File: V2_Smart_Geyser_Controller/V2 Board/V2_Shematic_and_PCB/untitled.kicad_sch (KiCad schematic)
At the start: 5 parts, among them J2 1714984, K2 SLA-12VDC-SL-C, Q1 AO3400A

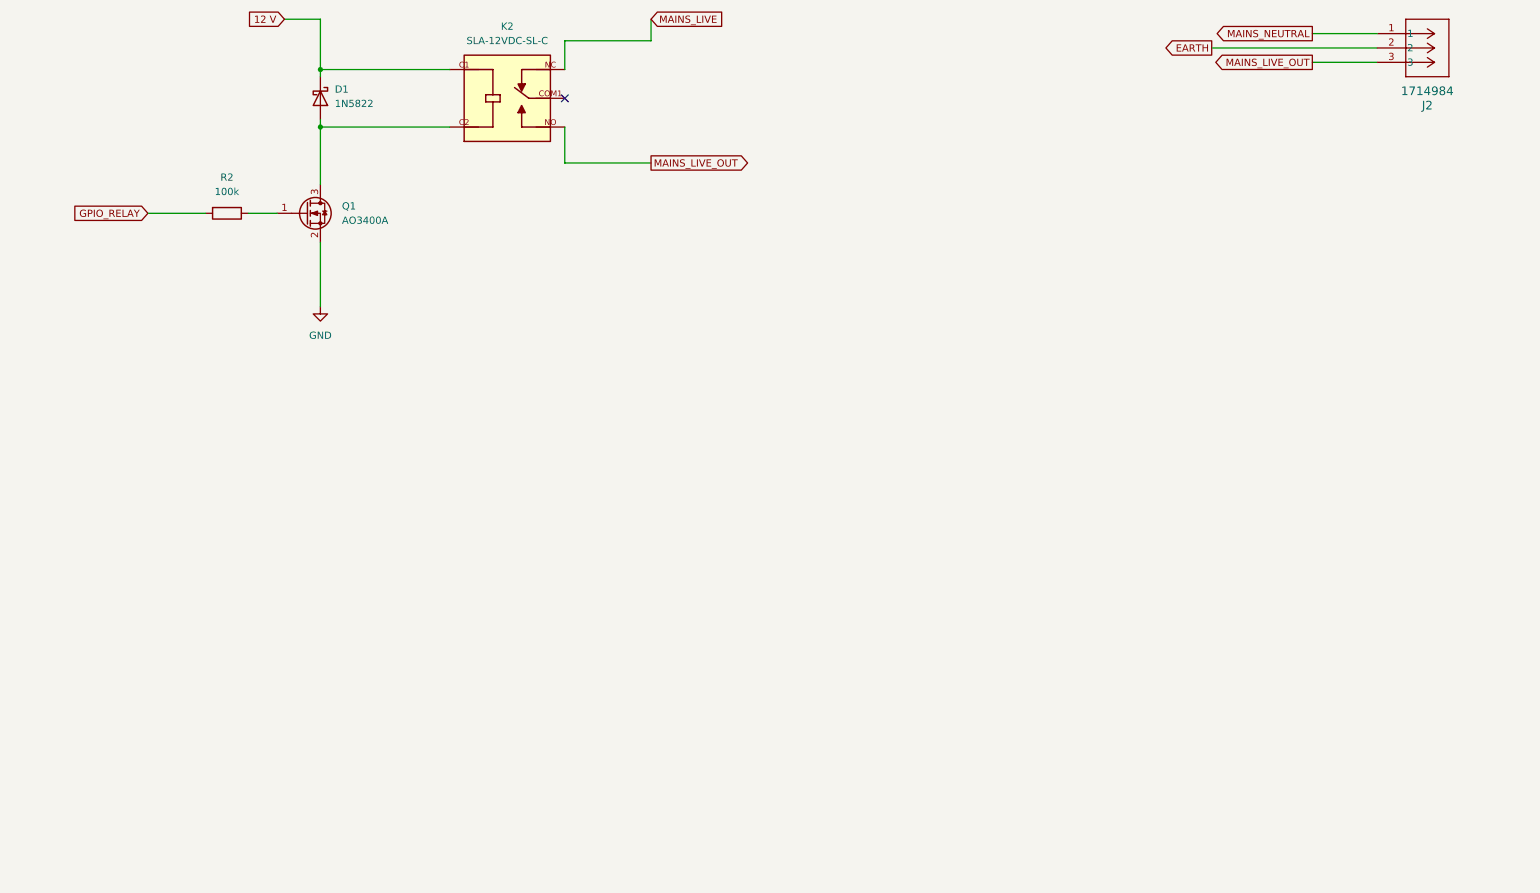
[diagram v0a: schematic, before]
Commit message: Added AC-1020 CT sensor circuit, annotation still needed
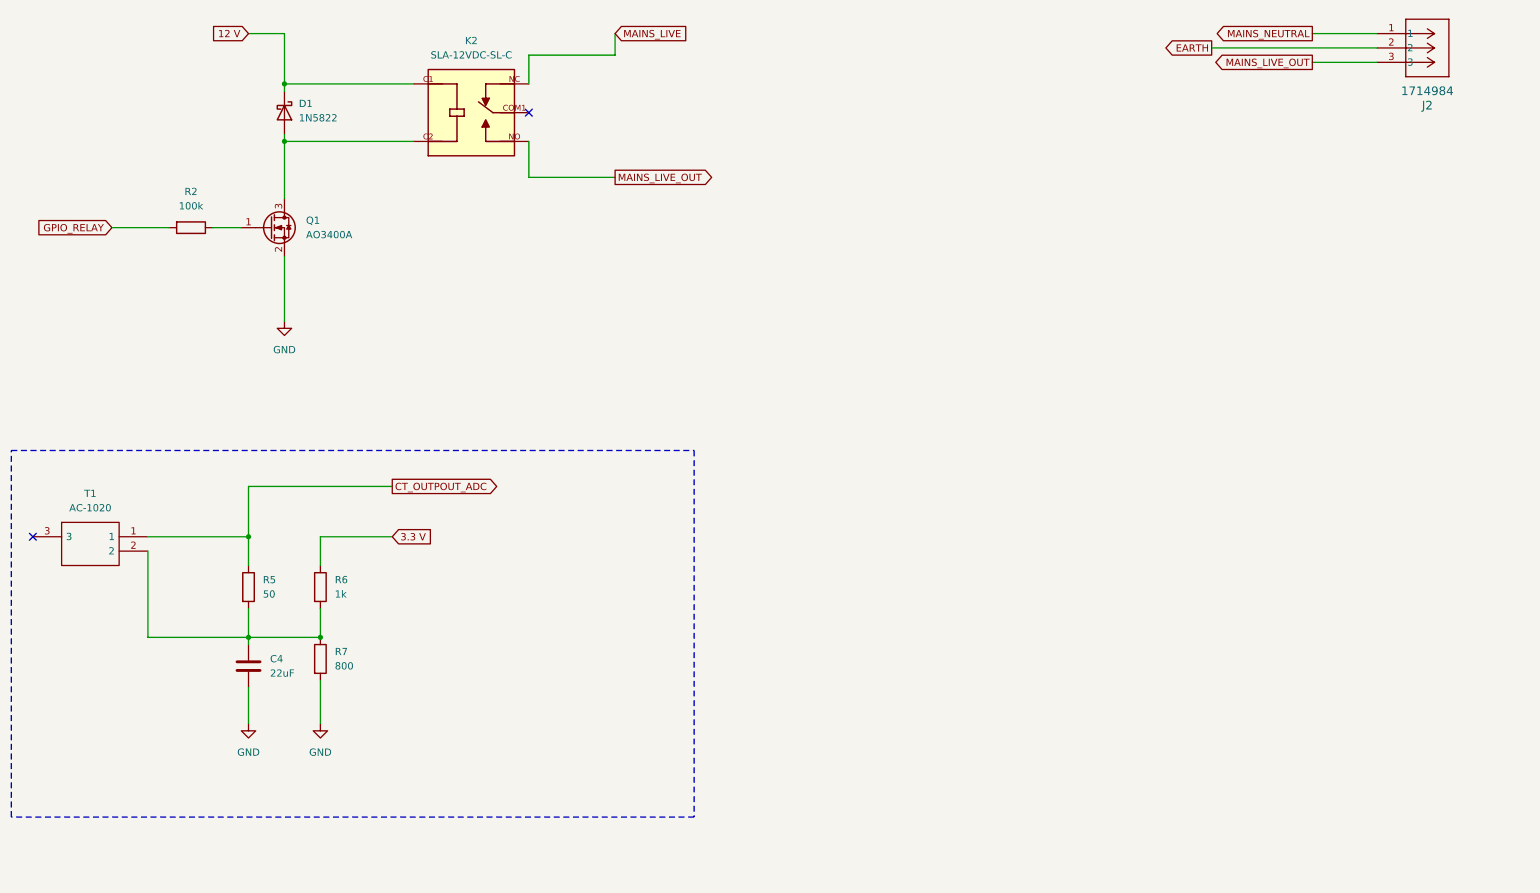
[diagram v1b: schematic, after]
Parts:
- added C4: 22uF, Capacitor_SMD:C_0805_2012Metric, symbol Device:C
- added R5: 50, Resistor_SMD:R_0805_2012Metric, symbol Device:R
- added R6: 1k, Resistor_SMD:R_0805_2012Metric, symbol Device:R
- added R7: 800, Resistor_SMD:R_0805_2012Metric, symbol Device:R
- added T1: AC-1020, AC1015, symbol AC-1020:AC-1020
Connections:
- net GND: now also C4.2, R7.2
- new net: C4.1, R5.2, R6.2, R7.1, T1.2
- new net 3.3 V: R6.1
- new net CT_OUTPOUT_ADC: R5.1, T1.1
- no-connect marks 1 -> 2
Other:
- moved on the sheet: D1, K2, Q1, R2

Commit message: Just an update
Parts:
- added Q2: AO3400A, Package_TO_SOT_SMD:SOT-23, symbol Transistor_FET:AO3400A
- added R8: 1k, Resistor_SMD:R_0805_2012Metric, symbol Device:R
- added TH1: Thermistor_NTC, symbol Device:Thermistor_NTC
- R2: value 100k -> 1k
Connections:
- net GND: now also Q2.2 (S); no longer Q1.2 (S)
- net GPIO_RELAY renamed GPIO1_RELAY
- new net: Q2.1 (G), R8.1
- new net: Q1.2 (S), Q2.3 (D)
- new net GPIO2_RELAY: R8.2

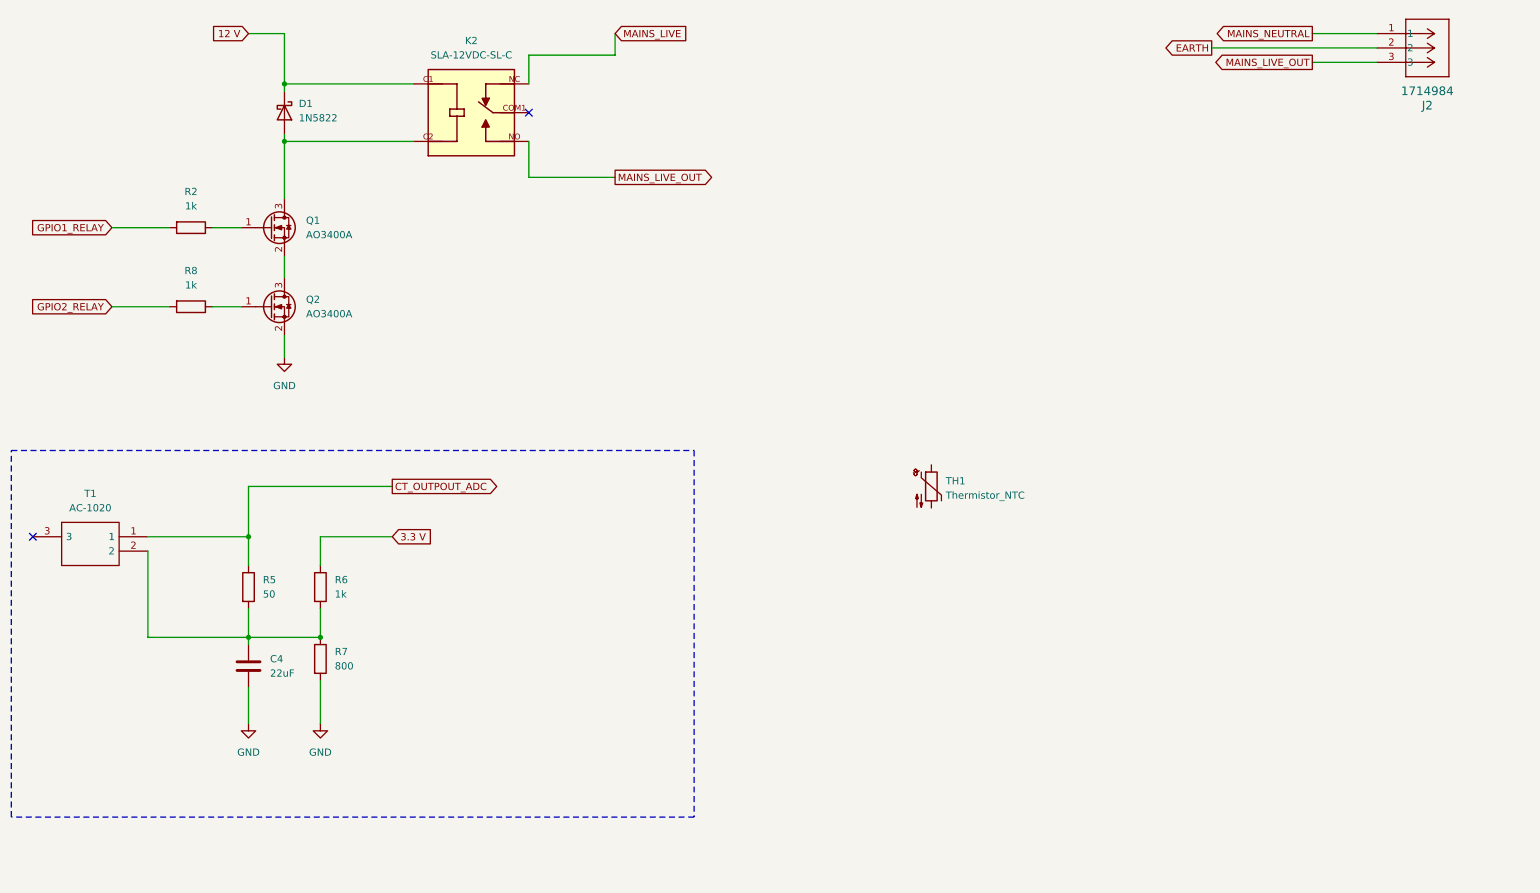
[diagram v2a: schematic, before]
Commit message: Added voltage transformer, circuit still need annotation
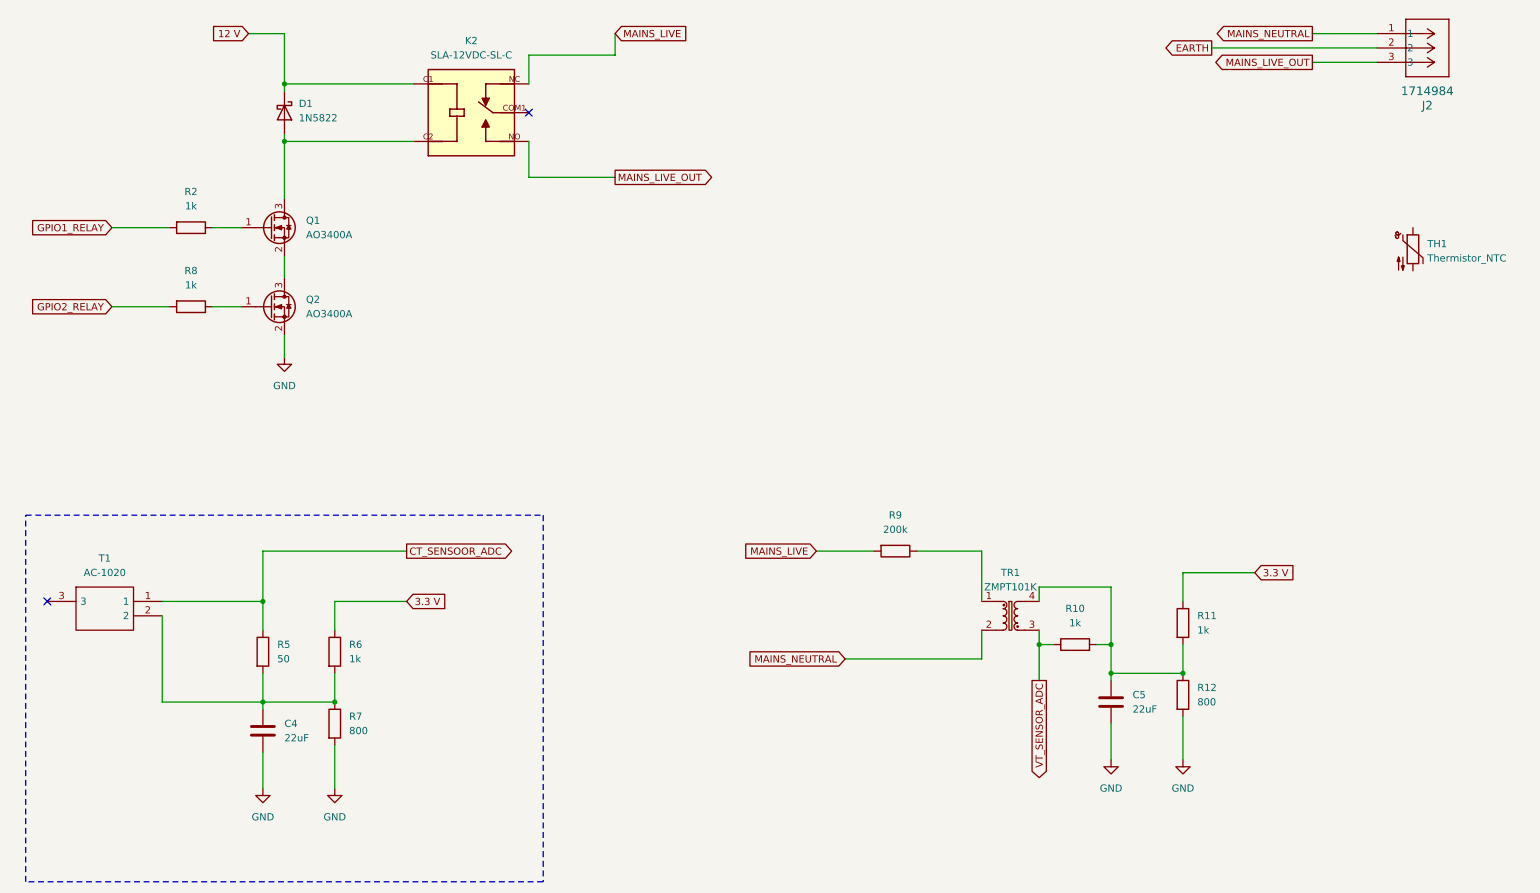
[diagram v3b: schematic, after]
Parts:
- added C5: 22uF, Capacitor_SMD:C_0805_2012Metric, symbol Device:C
- added R10, R11: 1k, Resistor_SMD:R_0805_2012Metric, symbol Device:R
- added R12: 800, Resistor_SMD:R_0805_2012Metric, symbol Device:R
- added R9: 200k, Resistor_SMD:R_0805_2012Metric, symbol Device:R
- added TR1: ZMPT101K, Transformer_THT:Transformer_Zeming_ZMPT101K, symbol Transformer:ZMPT101K
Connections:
- net 3.3 V: now also R11.1
- net GND: now also C5.2, R12.2
- net MAINS_LIVE: now also R9.2
- net MAINS_NEUTRAL: now also TR1.2
- net CT_OUTPOUT_ADC renamed CT_SENSOOR_ADC
- new net: C5.1, R10.2, R11.2, R12.1, TR1.4
- new net: R9.1, TR1.1
- new net VT_SENSOR_ADC: R10.1, TR1.3
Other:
- moved on the sheet: C4, R5, R6, R7, T1, TH1
